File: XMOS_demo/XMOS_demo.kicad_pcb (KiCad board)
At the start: 4 copper layers, 100 x 100 mm, 244 parts, among them J1 XSYS2 DEBUG CONNECTOR, J10 Conn_PMOD_02x06, J11 Conn_PMOD_02x06, J2 Screw_Terminal, J3 Conn_01x02_Pin, J4 USB_C_Receptacle_USB2.0_16P, J7 AudioJack3_SwitchT, J8 AudioJack2_SwitchT, J9 AudioJack2_SwitchT, U1 U316-1024-QF60B, U10 OPA340NA, U11 OPA340NA, U12 AT25FF161A, U13 OPA1637, U2 MAX97220C, U3 TPD3S014, U4 TLV75733PDBV, U5 TLV75718PDBV, U6 AP61200Z6, U7 OPA1637, U8 CS4271, U9 OPA340NA, Y1 Crystal_24M, Y2 24.576M

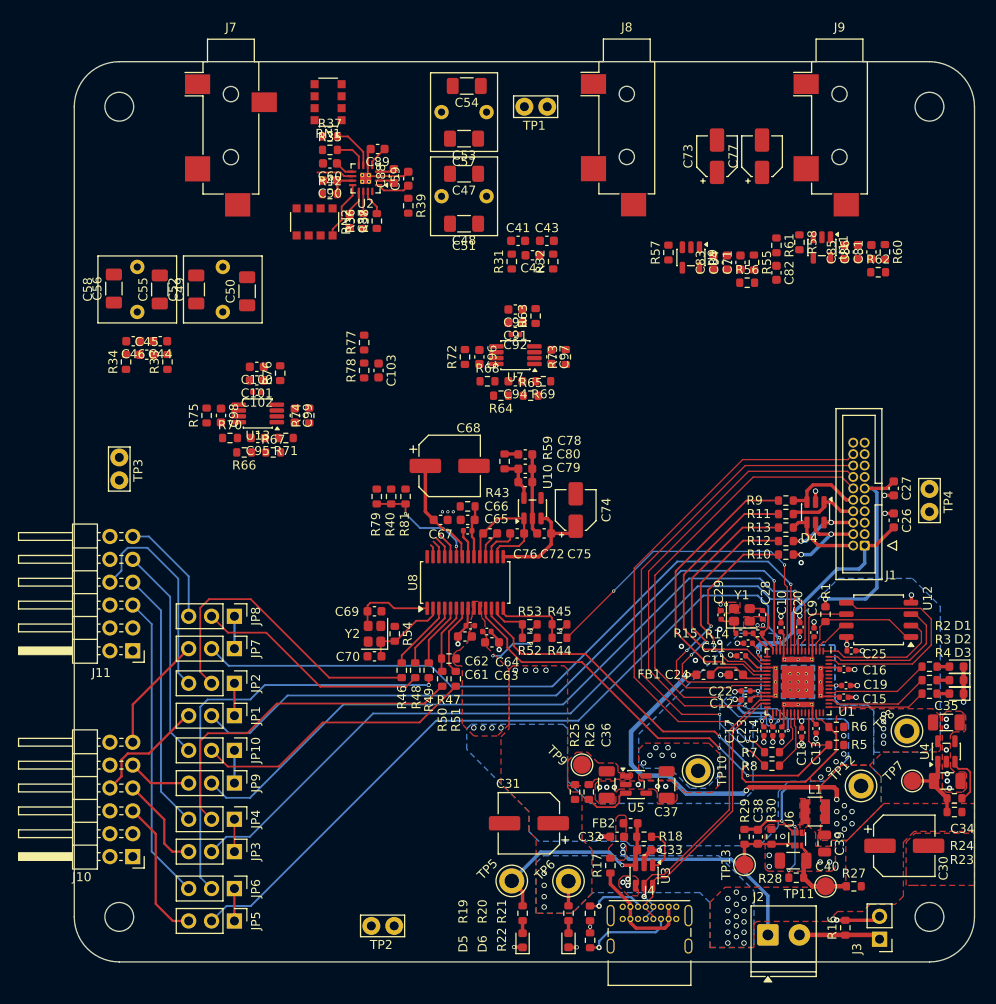
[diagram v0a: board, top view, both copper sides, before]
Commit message: work on pcb layout, added active filter to dac out
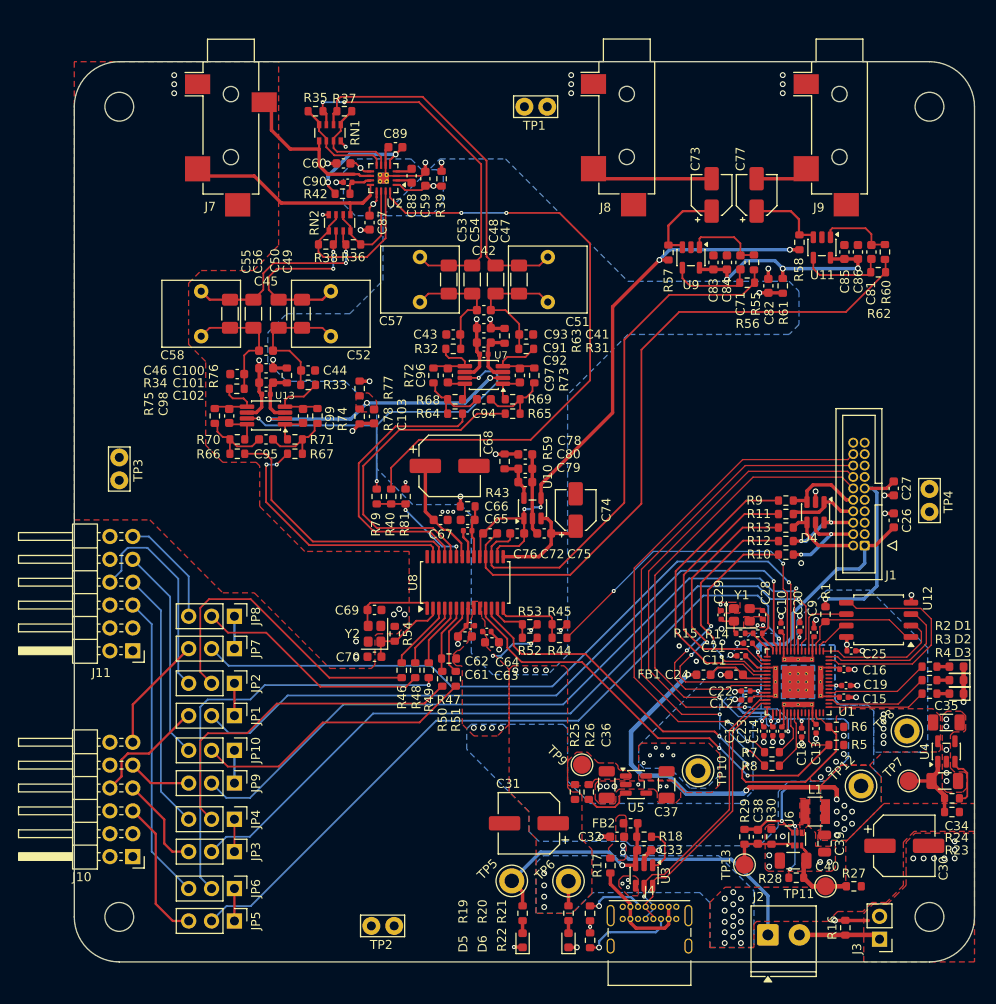
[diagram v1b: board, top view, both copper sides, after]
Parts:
- C90: footprint Capacitor_SMD:C_0603_1608Metric -> Capacitor_SMD:C_0402_1005Metric
- RN1, RN2: footprint Resistor_SMD:R_Array_Convex_4x1206 -> Resistor_SMD:R_Array_Convex_4x0603
- moved C57 22.4 mm to (130.4, 77.7), turned to 90 degrees
- moved C54 21.5 mm to (136.2, 75.2), turned to 90 degrees
- moved C44 16.7 mm to (118.0, 85.3)
- moved R33 15.8 mm to (118.0, 86.9), turned to 180 degrees
- moved C56 15.8 mm to (111.9, 79.0)
- moved C53 15.7 mm to (133.6, 75.2), turned to 90 degrees
- moved R32 14.7 mm to (134.1, 82.9), turned to 0 degrees
- moved C43 14.7 mm to (134.1, 81.3), turned to 180 degrees
- moved C51 13.6 mm to (144.6, 77.7), turned to 90 degrees
- moved C45 13.3 mm to (113.3, 83.1)
- moved C47 13.2 mm to (141.4, 75.2), turned to 90 degrees
- moved R34 12.7 mm to (110.1, 87.3), turned to 0 degrees
- moved C52 12.3 mm to (120.5, 81.5)
- moved C46 12.1 mm to (110.1, 85.7)
- moved C49 12.1 mm to (117.3, 79.0)
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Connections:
- RN1 pad 1: /Audio Out/AMP_INR- -> /Audio Out/AMP_INR+
- RN1 pad 2: /Audio Out/AMP_INR+ -> /Audio Out/R_INR+
- RN1 pad 3: /Audio Out/AMP_INR+ -> /Audio Out/R_INR-
- RN1 pad 5: /Audio Out/R_INR- -> /Audio Out/AMP_OUTR
- RN1 pad 6: /Audio Out/R_INR+ -> /Audio Out/AMP_INR-
- RN1 pad 7: GND -> /Audio Out/AMP_INR+
- RN1 pad 8: /Audio Out/AMP_OUTR -> GND
- RN2 pad 1: /Audio Out/AMP_INL- -> /Audio Out/AMP_INL+
- RN2 pad 2: /Audio Out/AMP_INL+ -> /Audio Out/R_INL+
- RN2 pad 3: /Audio Out/AMP_INL+ -> /Audio Out/R_INL-
- RN2 pad 5: /Audio Out/R_INL- -> /Audio Out/AMP_OUTL
- RN2 pad 6: /Audio Out/R_INL+ -> /Audio Out/AMP_INL-
- RN2 pad 7: GND -> /Audio Out/AMP_INL+
- RN2 pad 8: /Audio Out/AMP_OUTL -> GND
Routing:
- net /Audio In/AIN_B: track 3.12 -> 74.5 mm
- net /Audio Out/AMP_~{SHDN}: track 0.00 -> 68.7 mm, vias 0 -> 2
- net /Audio In/AIN_A: track 4.51 -> 60.0 mm
- net /Audio In/VQ2_3: track 15.4 -> 68.3 mm, vias 0 -> 4
- net /Output filter/OPA_~{PD}: track 0.00 -> 42.1 mm, vias 0 -> 3
- net /Audio Out/R_INR-: track 0.00 -> 40.9 mm, vias 0 -> 2
- net /Audio Out/R_INR+: track 0.00 -> 40.8 mm
- net /Codec/OUT_A-: track 3.01 -> 35.9 mm
- net /Codec/OUT_A+: track 2.48 -> 32.3 mm
- net /Output filter/OPA_OCM: track 0.00 -> 29.8 mm, vias 0 -> 3
- net /Codec/OUT_B+: track 1.94 -> 29.6 mm
- net /Codec/OUT_B-: track 1.39 -> 28.7 mm, vias 0 -> 2
- net P_OP1_SUPPLY: track 0.00 -> 25.3 mm, vias 0 -> 3
- net /Audio Out/R_INL-: track 0.00 -> 22.9 mm, vias 0 -> 2
- net GND: track 61.6 -> 84.1 mm, vias 61 -> 91
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- added copper zone on F.Cu, net /Output filter/OPA_OCM
- added copper zone on B.Cu, net P_AMP_SUPPLY
